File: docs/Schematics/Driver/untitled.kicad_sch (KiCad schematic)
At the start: 4 parts

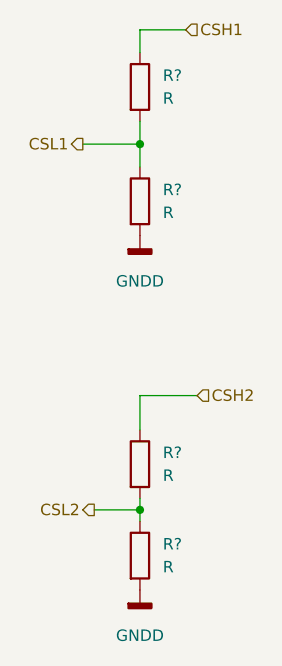
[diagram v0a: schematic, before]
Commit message: Added footprints and a symbol for the level shifters
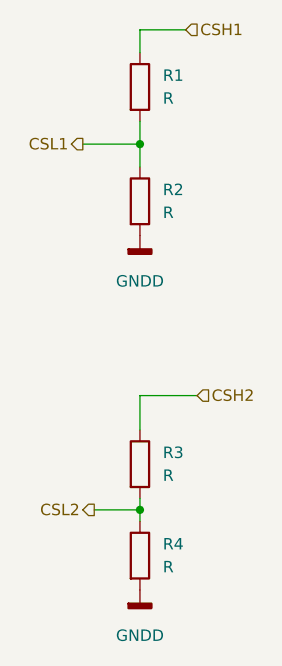
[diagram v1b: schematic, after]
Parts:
- R1, R2, R3, R4: renamed from R?; footprint (none) -> Resistor_THT:R_Axial_DIN0617_L17.0mm_D6.0mm_P25.40mm_Horizontal
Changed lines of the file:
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@@
   (symbol (lib_id "Device:R") (at 153.67 99.06 0) (unit 1)
     (in_bom yes) (on_board yes) (fields_autoplaced)
-    (property "Reference" "R?" (id 0) (at 156.21 97.7899 0)
+    (property "Reference" "R3" (id 0) (at 156.21 97.7899 0)
       (effects (font (size 1.27 1.27)) (justify left))
     )
@@
       (effects (font (size 1.27 1.27)) (justify left))
     )
-    (property "Footprint" "" (id 2) (at 151.892 99.06 90)
+    (property "Footprint" "Resistor_THT:R_Axial_DIN0617_L17.0mm_D6.0mm_P25.40mm_Horizontal" (id 2) (at 151.892 99.06 90)
       (effects (font (size 1.27 1.27)) hide)
     )
@@
   (symbol (lib_id "Device:R") (at 153.67 109.22 0) (unit 1)
     (in_bom yes) (on_board yes) (fields_autoplaced)
-    (property "Reference" "R?" (id 0) (at 156.21 107.9499 0)
+    (property "Reference" "R4" (id 0) (at 156.21 107.9499 0)
       (effects (font (size 1.27 1.27)) (justify left))
     )
@@
       (effects (font (size 1.27 1.27)) (justify left))
     )
-    (property "Footprint" "" (id 2) (at 151.892 109.22 90)
+    (property "Footprint" "Resistor_THT:R_Axial_DIN0617_L17.0mm_D6.0mm_P25.40mm_Horizontal" (id 2) (at 151.892 109.22 90)
       (effects (font (size 1.27 1.27)) hide)
     )
@@
   (symbol (lib_id "power:GNDD") (at 153.67 73.66 0) (unit 1)
     (in_bom yes) (on_board yes) (fields_autoplaced)
-    (property "Reference" "#PWR?" (id 0) (at 153.67 80.01 0)
+    (property "Reference" "#PWR052" (id 0) (at 153.67 80.01 0)
       (effects (font (size 1.27 1.27)) hide)
     )
@@
   (symbol (lib_id "Device:R") (at 153.67 57.15 0) (unit 1)
     (in_bom yes) (on_board yes) (fields_autoplaced)
-    (property "Reference" "R?" (id 0) (at 156.21 55.8799 0)
+    (property "Reference" "R1" (id 0) (at 156.21 55.8799 0)
       (effects (font (size 1.27 1.27)) (justify left))
     )
@@
       (effects (font (size 1.27 1.27)) (justify left))
     )
-    (property "Footprint" "" (id 2) (at 151.892 57.15 90)
+    (property "Footprint" "Resistor_THT:R_Axial_DIN0617_L17.0mm_D6.0mm_P25.40mm_Horizontal" (id 2) (at 151.892 57.15 90)
       (effects (font (size 1.27 1.27)) hide)
     )
@@
   (symbol (lib_id "power:GNDD") (at 153.67 113.03 0) (unit 1)
     (in_bom yes) (on_board yes) (fields_autoplaced)
-    (property "Reference" "#PWR?" (id 0) (at 153.67 119.38 0)
+    (property "Reference" "#PWR053" (id 0) (at 153.67 119.38 0)
       (effects (font (size 1.27 1.27)) hide)
     )
@@
   (symbol (lib_id "Device:R") (at 153.67 69.85 0) (unit 1)
     (in_bom yes) (on_board yes) (fields_autoplaced)
-    (property "Reference" "R?" (id 0) (at 156.21 68.5799 0)
+    (property "Reference" "R2" (id 0) (at 156.21 68.5799 0)
       (effects (font (size 1.27 1.27)) (justify left))
     )
@@
       (effects (font (size 1.27 1.27)) (justify left))
     )
-    (property "Footprint" "" (id 2) (at 151.892 69.85 90)
+    (property "Footprint" "Resistor_THT:R_Axial_DIN0617_L17.0mm_D6.0mm_P25.40mm_Horizontal" (id 2) (at 151.892 69.85 90)
       (effects (font (size 1.27 1.27)) hide)
     )

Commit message: Started routing the pcb.
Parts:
- R1, R2, R3, R4: footprint Resistor_THT:R_Axial_DIN0617_L17.0mm_D6.0mm_P25.40mm_Horizontal -> Resistor_THT:R_Axial_DIN0309_L9.0mm_D3.2mm_P15.24mm_Horizontal
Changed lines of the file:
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@@
       (effects (font (size 1.27 1.27)) (justify left))
     )
-    (property "Footprint" "Resistor_THT:R_Axial_DIN0617_L17.0mm_D6.0mm_P25.40mm_Horizontal" (id 2) (at 151.892 99.06 90)
+    (property "Footprint" "Resistor_THT:R_Axial_DIN0309_L9.0mm_D3.2mm_P15.24mm_Horizontal" (id 2) (at 151.892 99.06 90)
       (effects (font (size 1.27 1.27)) hide)
     )
@@
       (effects (font (size 1.27 1.27)) (justify left))
     )
-    (property "Footprint" "Resistor_THT:R_Axial_DIN0617_L17.0mm_D6.0mm_P25.40mm_Horizontal" (id 2) (at 151.892 109.22 90)
+    (property "Footprint" "Resistor_THT:R_Axial_DIN0309_L9.0mm_D3.2mm_P15.24mm_Horizontal" (id 2) (at 151.892 109.22 90)
       (effects (font (size 1.27 1.27)) hide)
     )
@@
       (effects (font (size 1.27 1.27)) (justify left))
     )
-    (property "Footprint" "Resistor_THT:R_Axial_DIN0617_L17.0mm_D6.0mm_P25.40mm_Horizontal" (id 2) (at 151.892 57.15 90)
+    (property "Footprint" "Resistor_THT:R_Axial_DIN0309_L9.0mm_D3.2mm_P15.24mm_Horizontal" (id 2) (at 151.892 57.15 90)
       (effects (font (size 1.27 1.27)) hide)
     )
@@
       (effects (font (size 1.27 1.27)) (justify left))
     )
-    (property "Footprint" "Resistor_THT:R_Axial_DIN0617_L17.0mm_D6.0mm_P25.40mm_Horizontal" (id 2) (at 151.892 69.85 90)
+    (property "Footprint" "Resistor_THT:R_Axial_DIN0309_L9.0mm_D3.2mm_P15.24mm_Horizontal" (id 2) (at 151.892 69.85 90)
       (effects (font (size 1.27 1.27)) hide)
     )

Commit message: First version of the routed board is done
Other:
- title: Arty Z7 IO expander card -> Arty Z7 IO Board
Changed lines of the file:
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@@
   (paper "A4")
   (title_block
-    (title "Arty Z7 IO expander card")
+    (title "Arty Z7 IO Board")
     (date "2022-12-24")
-    (rev "0.1")
+    (rev "${VER}")
     (company "HiQ")
   )
